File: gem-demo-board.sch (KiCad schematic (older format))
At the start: 146 parts, among them J1 3220-10-0100-00, J10 0473460001, J2 DF13A-2P-1.25H, J3 3220-10-0100-00, J4 2x20_Header_Female, J5 0473460001, J6 556500488, J7 556500488, J8 WE_686115148922, J9 WE_686115148922_FLIPPED, U1 MCP1700T-3302E_TT, U2 NTS0104BQ, U3 NTS0104BQ, U4 NTS0104BQ, U5 93LC56CT-IMC, U6 FT4232HQ, U7 NTB0104BQ, U8 NTB0104BQ, Y1 ASFLMB-12.000MHZ-LC-T

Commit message: Updated README
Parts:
- removed N1: antmicro_logo, zglue-demo-board-footprints:antmicro-logo, symbol zglue-demo-board:antmicro_logo
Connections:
- wire segments 522 -> 510
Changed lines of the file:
@@
 encoding utf-8
 Sheet 1 1
-Title "zGlue Demo Board"
+Title "GEM Demo Board"
 Date ""
 Rev "1.1"
@@
 Wire Wire Line
 	11900 9650 11750 9650
-Connection ~ 11750 9650
 Text Label 1250 1100 0    50   ~ 0
 5V0_IN
@@
 	1    0    0    -1
 $EndComp
-Wire Wire Line
-	2050 8550 2100 8550
 Text Label 2250 8550 0    50   ~ 0
 VPLL
@@
 PROG_USB_D_P
 Wire Wire Line
-	2050 8000 2100 8000
-Wire Wire Line
 	2750 8550 2750 8100
 Wire Wire Line
@@
 	1    0    0    -1
 $EndComp
-Connection ~ 2500 8000
-Wire Wire Line
-	2500 8000 4100 8000
 $Comp
 L zglue-demo-board:C_4u7_0402 C26
@@
 	1    0    0    -1
 $EndComp
-Connection ~ 2500 8550
-Wire Wire Line
-	2500 8550 2750 8550
 $Comp
 L zglue-demo-board:C_100n_0402_6V3 C21
@@
 	1    0    0    -1
 $EndComp
-Connection ~ 2100 8000
-Wire Wire Line
-	2100 8000 2500 8000
 $Comp
 L zglue-demo-board:C_100n_0402_6V3 C22
@@
 	1    0    0    -1
 $EndComp
-Connection ~ 2100 8550
-Wire Wire Line
-	2100 8550 2500 8550
 $Comp
 L zglue-demo-board:GND #PWR037
@@
 	2400 6250 2400 6300
 Connection ~ 2000 6250
-Wire Wire Line
-	2400 6600 2000 6600
-Connection ~ 1150 6600
-Connection ~ 1550 6600
-Wire Wire Line
-	1550 6600 1150 6600
-Connection ~ 2000 6600
-Wire Wire Line
-	2000 6600 1550 6600
 $Comp
 L zglue-demo-board:0473460001 J10
@@
 	1    0    0    -1
 $EndComp
-Connection ~ 2000 7250
 Text Label 1600 6900 0    50   ~ 0
 1V8_FTDI
@@
 Wire Wire Line
 	3450 9350 4100 9350
-Wire Wire Line
-	1900 10150 2300 10150
-Connection ~ 2300 10150
-Wire Wire Line
-	2300 10150 3150 10150
-Connection ~ 3150 10150
-Wire Wire Line
-	3150 10150 3450 10150
 $Comp
 L zglue-demo-board:ASFLMB-12.000MHZ-LC-T Y1
@@
 Wire Wire Line
 	1200 10950 1200 10500
-Connection ~ 1500 10950
 $Comp
 L zglue-demo-board:FT4232HQ U6
@@
 Text Notes 3250 850  0    79   ~ 16
 Voltage level selection
-$Comp
-L zglue-demo-board:antmicro_logo N1
-U 1 1 5DEA001B
-P 12450 10200
-F 0 "N1" H 12500 10461 50  0001 C CNN
-F 1 "antmicro_logo" H 12500 10462 50  0001 C CNN
-F 2 "zglue-demo-board-footprints:antmicro-logo" H 12350 10450 50  0001 C CNN
-F 3 "" H 12450 10550 50  0001 C CNN
-	1    12450 10200
-	1    0    0    -1
-$EndComp
 Wire Wire Line
 	4550 5700 3900 5700
@@
 $EndComp
 Wire Wire Line
-	7950 10200 7300 10200
-Connection ~ 6600 10200
-Wire Wire Line
-	6600 10200 6050 10200
-Connection ~ 7300 10200
-Wire Wire Line
-	7300 10200 6600 10200
-Wire Wire Line
 	7250 9250 7250 9350
 Wire Wire Line
@@
 3V3_SYS
 Wire Wire Line
-	7950 8950 7250 8950
-Connection ~ 7250 8950
-Connection ~ 6600 8950
-Wire Wire Line
-	6600 8950 7250 8950
-Wire Wire Line
-	6000 8950 6600 8950
-Wire Wire Line
 	6600 9650 5950 9650
 Wire Wire Line
@@
 Text Label 13250 850  0    50   ~ 0
 VUSB
+Wire Wire Line
+	2050 8000 4100 8000
+Wire Wire Line
+	2050 8550 2750 8550
+Wire Wire Line
+	1150 6600 2400 6600
+Wire Wire Line
+	1900 10150 3450 10150
+Wire Wire Line
+	6050 10200 7950 10200
+Wire Wire Line
+	6000 8950 7950 8950
 $EndSCHEMATC

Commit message: Flipped CSI input connector
Use camera FFC with pads on the same side now
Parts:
- removed J8: WE_686115148922, zglue-demo-board-footprints:WE_686115148922, symbol zglue-demo-board:WE_686115148922
- added J8: WE_686115148922_FLIPPED, zglue-demo-board-footprints:WE_686115148922_FLIPPED, symbol zglue-demo-board:WE_686115148922_FLIPPED
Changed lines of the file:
@@
 Wire Wire Line
 	9400 10850 9400 10900
-$Comp
-L zglue-demo-board:WE_686115148922 J8
-U 1 1 5DE5416C
-P 15250 7000
-F 0 "J8" H 15150 6450 50  0000 L CNN
-F 1 "WE_686115148922" H 15100 6350 50  0000 L CNN
-F 2 "zglue-demo-board-footprints:WE_686115148922" H 13900 6350 50  0001 C CNN
-F 3 "https://katalog.we-online.com/em/datasheet/686115148922.pdf" H 14750 6250 50  0001 C CNN
-F 4 "686115148922" H 16200 6350 60  0001 L CNN "MPN"
-F 5 "Wurth Elektronik " H 15100 6350 60  0001 L CNN "Manufacturer"
-	1    15250 7000
-	1    0    0    -1
-$EndComp
 Wire Wire Line
 	15050 6000 14900 6000
@@
 Wire Wire Line
 	6000 8950 7950 8950
+$Comp
+L zglue-demo-board:WE_686115148922_FLIPPED J8
+U 1 1 5E13C0CF
+P 15250 7000
+F 0 "J8" H 15150 6450 50  0000 L CNN
+F 1 "WE_686115148922_FLIPPED" H 15000 6350 50  0000 L CNN
+F 2 "zglue-demo-board-footprints:WE_686115148922_FLIPPED" H 13900 6350 50  0001 C CNN
+F 3 "https://katalog.we-online.com/em/datasheet/686115148922.pdf" H 14750 6250 50  0001 C CNN
+F 4 "686115148922" H 16200 6350 60  0001 L CNN "MPN"
+F 5 "Wurth Elektronik " H 15100 6350 60  0001 L CNN "Manufacturer"
+	1    15250 7000
+	1    0    0    -1
+$EndComp
 $EndSCHEMATC

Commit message: Minor changes
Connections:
- net labels removed: CAM_GPIO_IN
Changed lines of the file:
@@
 Connection ~ 14900 6900
 Wire Wire Line
-	15050 7000 14100 7000
-Wire Wire Line
 	15050 7100 14100 7100
 Wire Wire Line
@@
 Wire Wire Line
 	1400 3850 850  3850
-Text Label 14200 7000 0    50   ~ 0
-CAM_GPIO_IN
 Text Label 14200 7100 0    50   ~ 0
 CAM_CLK_IN
@@
 1V8_SYS
 Wire Wire Line
-	13600 4200 12850 4200
-Wire Wire Line
 	13600 4300 12850 4300
 Wire Wire Line
+	13600 4200 12850 4200
+Wire Wire Line
 	15550 4200 14800 4200
 Wire Wire Line
@@
 NoConn ~ 14800 4400
 NoConn ~ 14800 4500
-Text Label 12900 4200 0    50   ~ 0
-DBG_TX
 Text Label 12900 4300 0    50   ~ 0
+DBG_TX
+Text Label 12900 4200 0    50   ~ 0
 DBG_RX
 Text Label 15050 4300 0    50   ~ 0
@@
 	1    0    0    -1
 $EndComp
+Wire Wire Line
+	15050 7000 14100 7000
+Text Label 14200 7000 0    50   ~ 0
+3V3_SYS
 $EndSCHEMATC

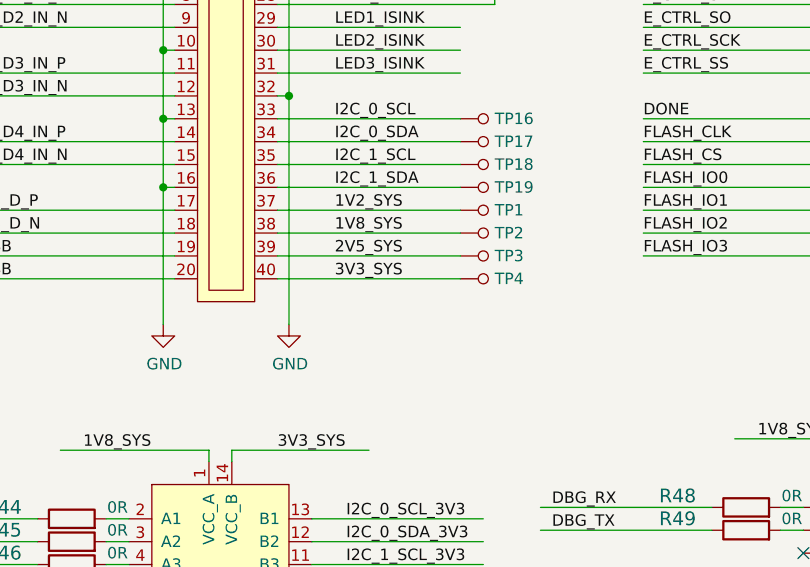
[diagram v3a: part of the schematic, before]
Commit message: Disconnected 3v3_sys from GEM system chip with R60
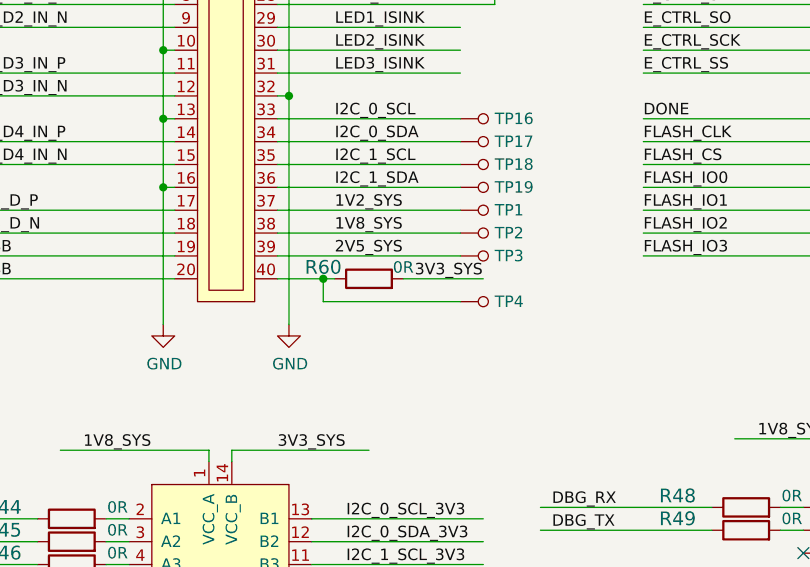
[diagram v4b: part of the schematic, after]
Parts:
- added R60: R_0R_0402, zglue-demo-board-footprints:0402-res, symbol zglue-demo-board:R_0R_0402
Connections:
- wire segments 510 -> 514
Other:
- moved on the sheet: TP4
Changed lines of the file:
@@
 Text Label 10350 3200 0    50   ~ 0
 VUSB
-Text Label 11950 3200 0    50   ~ 0
+Text Label 12300 3200 0    50   ~ 0
 3V3_SYS
 Text Label 11950 3000 0    50   ~ 0
@@
 Wire Wire Line
 	11700 3100 12500 3100
-Wire Wire Line
-	11700 3200 12500 3200
 Text Notes 10350 700  0    79   ~ 16
 Baseboard connectors
@@
 L zglue-demo-board:TP_SMD1MM TP4
 U 1 1 5DD625D6
-P 12600 3200
-F 0 "TP4" V 12600 3150 50  0000 R CNN
-F 1 "TP_SMD1MM" H 12600 3100 50  0001 C CNN
-F 2 "zglue-demo-board-footprints:Testpoint_smd_1mm" H 12800 3400 60  0001 L CNN
-F 3 "" H 12800 3500 60  0001 L CNN
-	1    12600 3200
+P 12600 3300
+F 0 "TP4" V 12600 3250 50  0000 R CNN
+F 1 "TP_SMD1MM" H 12600 3200 50  0001 C CNN
+F 2 "zglue-demo-board-footprints:Testpoint_smd_1mm" H 12800 3500 60  0001 L CNN
+F 3 "" H 12800 3600 60  0001 L CNN
+	1    12600 3300
 	0    -1   -1   0
 $EndComp
@@
 Text Label 14200 7000 0    50   ~ 0
 3V3_SYS
+$Comp
+L zglue-demo-board:R_0R_0402 R60
+U 1 1 5E59B2E4
+P 12100 3200
+F 0 "R60" H 11900 3250 60  0000 C CNN
+F 1 "R_0R_0402" H 12100 3050 60  0001 C CNN
+F 2 "zglue-demo-board-footprints:0402-res" H 12300 3400 60  0001 L CNN
+F 3 "" H 12100 3200 50  0001 C CNN
+F 4 "PANASONIC" H 12300 3600 60  0001 L CNN "Manufacturer"
+F 5 "ERJ2GE0R00X" H 12300 3500 60  0001 L CNN "MPN"
+F 6 "0R" H 12250 3250 50  0000 C CNN "Val"
+	1    12100 3200
+	1    0    0    -1
+$EndComp
+Wire Wire Line
+	11700 3200 11900 3200
+Wire Wire Line
+	12250 3200 12600 3200
+Wire Wire Line
+	12500 3300 11900 3300
+Wire Wire Line
+	11900 3300 11900 3200
+Connection ~ 11900 3200
+Wire Wire Line
+	11900 3200 11950 3200
 $EndSCHEMATC

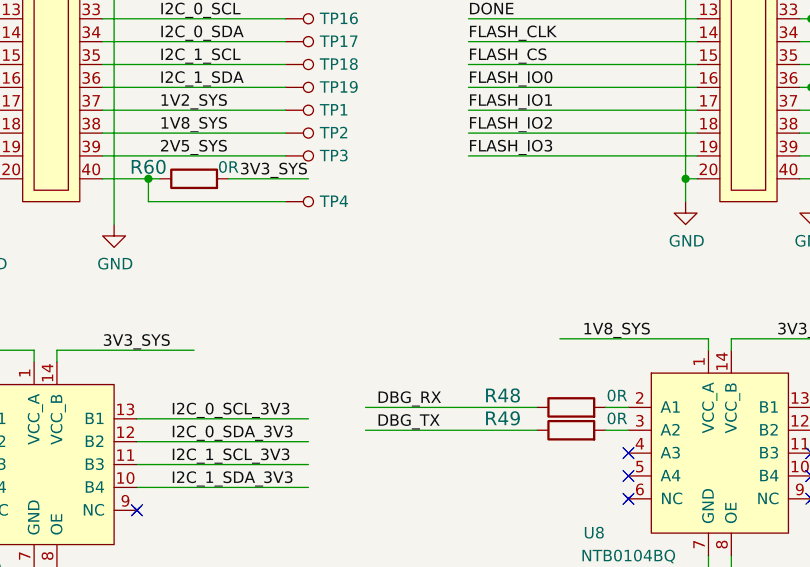
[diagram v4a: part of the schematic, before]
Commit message: Connect CSI_D1_IN_P to I2C_1_SDA through R61
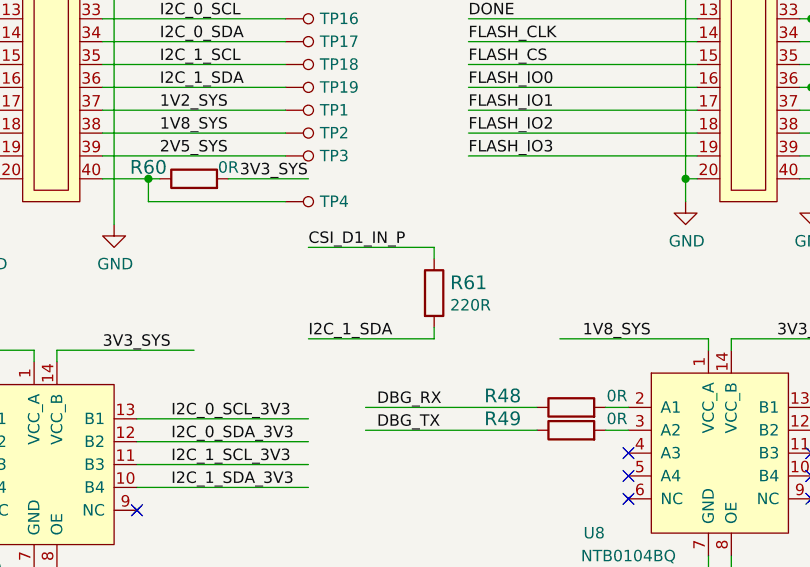
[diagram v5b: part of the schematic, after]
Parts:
- added R61: R_220R_0402, antmicro-footprints:0402-res, symbol antmicroResistors0402:R_220R_0402
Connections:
- wire segments 514 -> 518
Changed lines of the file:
@@
 Wire Wire Line
 	11900 3200 11950 3200
+Text Label 12600 3500 0    50   ~ 0
+CSI_D1_IN_P
+Wire Wire Line
+	13150 3500 12600 3500
+Text Label 12600 3900 0    50   ~ 0
+I2C_1_SDA
+Wire Wire Line
+	12600 3900 13150 3900
+$Comp
+L antmicroResistors0402:R_220R_0402 R61
+U 1 1 5EACC300
+P 13150 3700
+F 0 "R61" V 13105 3770 60  0000 L CNN
+F 1 "R_220R_0402" H 13150 3550 60  0001 C CNN
+F 2 "antmicro-footprints:0402-res" H 13350 3900 60  0001 L CNN
+F 3 "" H 13150 3700 50  0001 C CNN
+F 4 "TE_CONNECTIVITY_/_NEOHM" H 13350 4100 60  0001 L CNN "Manufacturer"
+F 5 "CRG0402J220R" H 13350 4000 60  0001 L CNN "MPN"
+F 6 "220R" V 13203 3770 50  0000 L CNN "Val"
+	1    13150 3700
+	0    1    1    0
+$EndComp
+Wire Wire Line
+	13150 3500 13150 3550
+Wire Wire Line
+	13150 3850 13150 3900
 $EndSCHEMATC

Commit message: Exported R_220R to local library
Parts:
- C1, C2, C3, C4, C5: symbol zglue-demo-board:C_1u_0603 -> gem-demo-board:C_1u_0603
- C10, C11, C12, C13, C14, C15, C16, C17, C18, C19, C20, C21, C22, C23, C24, C9: symbol zglue-demo-board:C_100n_0402_6V3 -> gem-demo-board:C_100n_0402_6V3
- C25, C26: symbol zglue-demo-board:C_4u7_0402 -> gem-demo-board:C_4u7_0402
- D1, D3, D4: symbol zglue-demo-board:MBR0540T1G -> gem-demo-board:MBR0540T1G
- D10, D11, D12, D13, D6, D7, D8, D9: symbol zglue-demo-board:LG_L29K-G2J1-24-Z -> gem-demo-board:LG_L29K-G2J1-24-Z
- D2, D5: symbol zglue-demo-board:TPD2EUSB30DRTR -> gem-demo-board:TPD2EUSB30DRTR
- FB1, FB2: symbol zglue-demo-board:BLM18AG601SN1D -> gem-demo-board:BLM18AG601SN1D
- J1, J3: symbol zglue-demo-board:3220-10-0100-00 -> gem-demo-board:3220-10-0100-00
- J10, J5: symbol zglue-demo-board:0473460001 -> gem-demo-board:0473460001
- J2: symbol zglue-demo-board:DF13A-2P-1.25H -> gem-demo-board:DF13A-2P-1.25H
- J4: symbol zglue-demo-board:2x20_Header_Female -> gem-demo-board:2x20_Header_Female
- J6, J7: symbol zglue-demo-board:556500488 -> gem-demo-board:556500488
- J8, J9: symbol zglue-demo-board:WE_686115148922_FLIPPED -> gem-demo-board:WE_686115148922_FLIPPED
- N2: symbol zglue-demo-board:zglue_logo -> gem-demo-board:zglue_logo
- N3: symbol zglue-demo-board:oshw_logo -> gem-demo-board:oshw_logo
- R1: symbol zglue-demo-board:R_0R_0603 -> gem-demo-board:R_0R_0603
- R10, R5: symbol zglue-demo-board:R_2k_0402 -> gem-demo-board:R_2k_0402
- R11, R12, R13, R14, R15, R16, R17, R18, R19, R2, R20, R21, R22, R23, R24, R25, R26, R27, R28, R29, R3, R30, R31, R32, R33, R42, R43, R44, R45, R46, R47, R48, R49, R50, R51, R52, R53, R54, R55, R56, R57, R58, R59, R60, R8: symbol zglue-demo-board:R_0R_0402 -> gem-demo-board:R_0R_0402
- R34: symbol zglue-demo-board:R_470R_0402 -> gem-demo-board:R_470R_0402
- R35, R36, R37, R38, R39, R40, R41: symbol zglue-demo-board:R_330R_0402 -> gem-demo-board:R_330R_0402
- R4, R6, R7: symbol zglue-demo-board:R_10k_0402 -> gem-demo-board:R_10k_0402
- R61: footprint antmicro-footprints:0402-res -> gem-demo-board-footprints:0402-res; symbol antmicroResistors0402:R_220R_0402 -> gem-demo-board:R_220R_0402
- R9: symbol zglue-demo-board:R_12k_0402 -> gem-demo-board:R_12k_0402
- S1: symbol zglue-demo-board:EVQPUA02K -> gem-demo-board:EVQPUA02K
- TP1, TP10, TP11, TP12, TP13, TP14, TP15, TP16, TP17, TP18, TP19, TP2, TP20, TP21, TP22, TP23, TP3, TP4, TP5, TP6, TP7, TP8, TP9: symbol zglue-demo-board:TP_SMD1MM -> gem-demo-board:TP_SMD1MM
- U1: symbol zglue-demo-board:MCP1700T-3302E_TT -> gem-demo-board:MCP1700T-3302E_TT
- U2, U3, U4: symbol zglue-demo-board:NTS0104BQ -> gem-demo-board:NTS0104BQ
- U5: symbol zglue-demo-board:93LC56CT-IMC -> gem-demo-board:93LC56CT-IMC
- U6: symbol zglue-demo-board:FT4232HQ -> gem-demo-board:FT4232HQ
- U7, U8: symbol zglue-demo-board:NTB0104BQ -> gem-demo-board:NTB0104BQ
- VCCIO1, VCCIO2, VCCIO3: symbol zglue-demo-board:Jumper_3_Open-Jumper -> gem-demo-board:Jumper_3_Open-Jumper
- Y1: symbol zglue-demo-board:ASFLMB-12.000MHZ-LC-T -> gem-demo-board:ASFLMB-12.000MHZ-LC-T

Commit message: Cleanup of DRC issues
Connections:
- net labels removed: RPI_DBG_RX_3V3, RPI_DBG_TX_3V3
- wire segments 518 -> 530
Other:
- moved on the sheet: C21, C25, D10, D11, D12, D13, D8, D9, FB1, R4, R6, R7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

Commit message: Minor updates on PCB
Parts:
- C1, C2, C3, C4, C5: footprint zglue-demo-board-footprints:0603-cap -> gem-demo-board-footprints:0603-cap
- C10, C11, C12, C13, C14, C15, C16, C17, C18, C19, C20, C21, C22, C23, C24, C25, C26, C9: footprint zglue-demo-board-footprints:0402-cap -> gem-demo-board-footprints:0402-cap
- D1, D3, D4: footprint zglue-demo-board-footprints:SOD-123 -> gem-demo-board-footprints:SOD-123
- D10, D11, D12, D13, D6, D7, D8, D9: footprint zglue-demo-board-footprints:LED_0603 -> gem-demo-board-footprints:LED_0603
- D2, D5: footprint zglue-demo-board-footprints:SOT-3 -> gem-demo-board-footprints:SOT-3
- FB1, FB2: footprint zglue-demo-board-footprints:0603 -> gem-demo-board-footprints:0603
- J1, J3: footprint zglue-demo-board-footprints:PinHeader_2x5_P1.27mm_Drill.7mm -> gem-demo-board-footprints:PinHeader_2x5_P1.27mm_Drill.7mm
- J10, J5: footprint zglue-demo-board-footprints:USB_Micro_B_Female_0473460001 -> gem-demo-board-footprints:USB_Micro_B_Female_0473460001
- J2: footprint zglue-demo-board-footprints:DF13A-2P-1.25H -> gem-demo-board-footprints:DF13A-2P-1.25H
- J4: footprint zglue-demo-board-footprints:PinHeader_2x40_P2.54_Drill1mm -> gem-demo-board-footprints:PinHeader_2x40_P2.54_Drill1mm
- J6, J7: footprint zglue-demo-board-footprints:556500488 -> gem-demo-board-footprints:556500488
- J8, J9: footprint zglue-demo-board-footprints:WE_686115148922_FLIPPED -> gem-demo-board-footprints:WE_686115148922_FLIPPED
- N2: footprint zglue-demo-board-footprints:zglue-logo -> gem-demo-board-footprints:zglue-logo
- N3: footprint zglue-demo-board-footprints:oshw-logo -> gem-demo-board-footprints:oshw-logo
- R1: footprint zglue-demo-board-footprints:0603-res -> gem-demo-board-footprints:0603-res
- R10, R11, R12, R13, R14, R15, R16, R17, R18, R19, R2, R20, R21, R22, R23, R24, R25, R26, R27, R28, R29, R3, R30, R31, R32, R33, R34, R35, R36, R37, R38, R39, R4, R40, R41, R42, R43, R44, R45, R46, R47, R48, R49, R5, R50, R51, R52, R53, R54, R55, R56, R57, R58, R59, R6, R60, R7, R8, R9: footprint zglue-demo-board-footprints:0402-res -> gem-demo-board-footprints:0402-res
- S1: footprint zglue-demo-board-footprints:Panasonic_EVQPUJ_EVQPUA -> gem-demo-board-footprints:Panasonic_EVQPUJ_EVQPUA
- TP1, TP10, TP11, TP12, TP13, TP14, TP15, TP16, TP17, TP18, TP19, TP2, TP20, TP21, TP22, TP23, TP3, TP4, TP5, TP6, TP7, TP8, TP9: footprint zglue-demo-board-footprints:Testpoint_smd_1mm -> gem-demo-board-footprints:Testpoint_smd_1mm
- U1: footprint zglue-demo-board-footprints:SOT-23-3 -> gem-demo-board-footprints:SOT-23-3
- U2, U3, U4, U7, U8: footprint zglue-demo-board-footprints:QDHVQFN14 -> gem-demo-board-footprints:QDHVQFN14
- U5: footprint zglue-demo-board-footprints:DFN-8_2x3mm -> gem-demo-board-footprints:DFN-8_2x3mm
- U6: footprint zglue-demo-board-footprints:FT4232HQ -> gem-demo-board-footprints:FT4232HQ
- Y1: footprint zglue-demo-board-footprints:ASFLMB -> gem-demo-board-footprints:ASFLMB
